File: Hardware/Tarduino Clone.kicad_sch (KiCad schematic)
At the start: 20 parts, among them J1 Conn_01x07_Male, J2 Conn_01x04_Male, J3 Conn_01x02_Male, J4 Conn_01x02_Male, J5 Conn_01x02_Male, J6 Conn_01x02_Male, J7 Conn_01x08_Male, J8 QWIIC_Vertical, J9 QWIIC_Stackable, SW1 SW_Push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

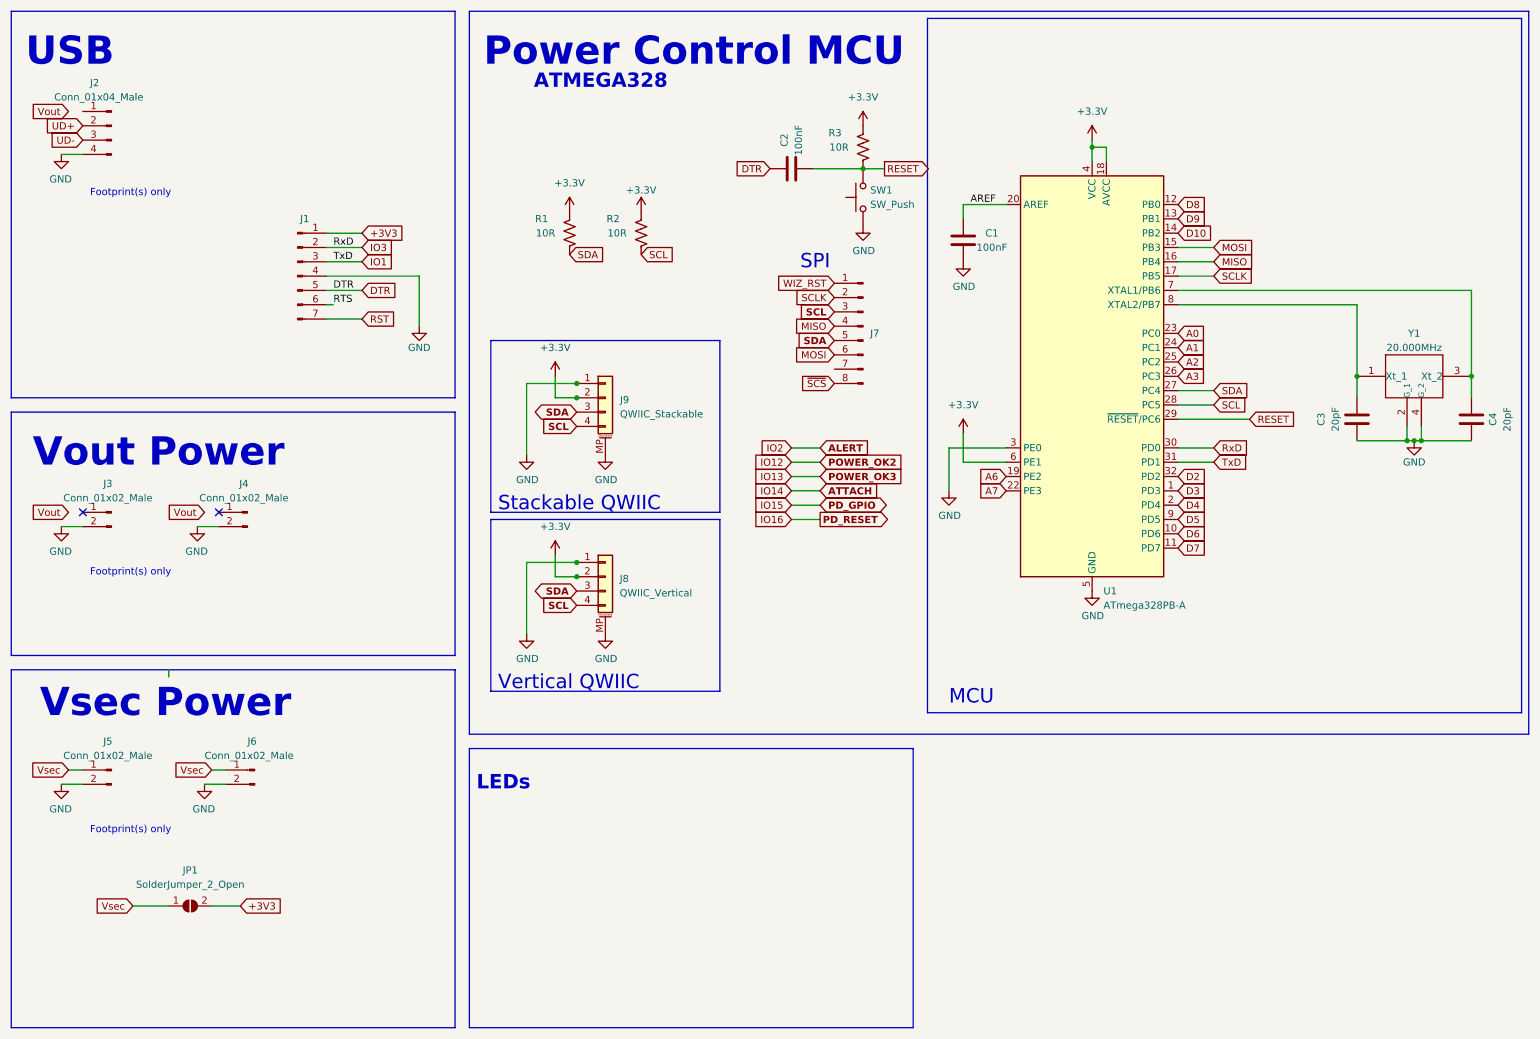
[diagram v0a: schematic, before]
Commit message: Still cleaning up J7
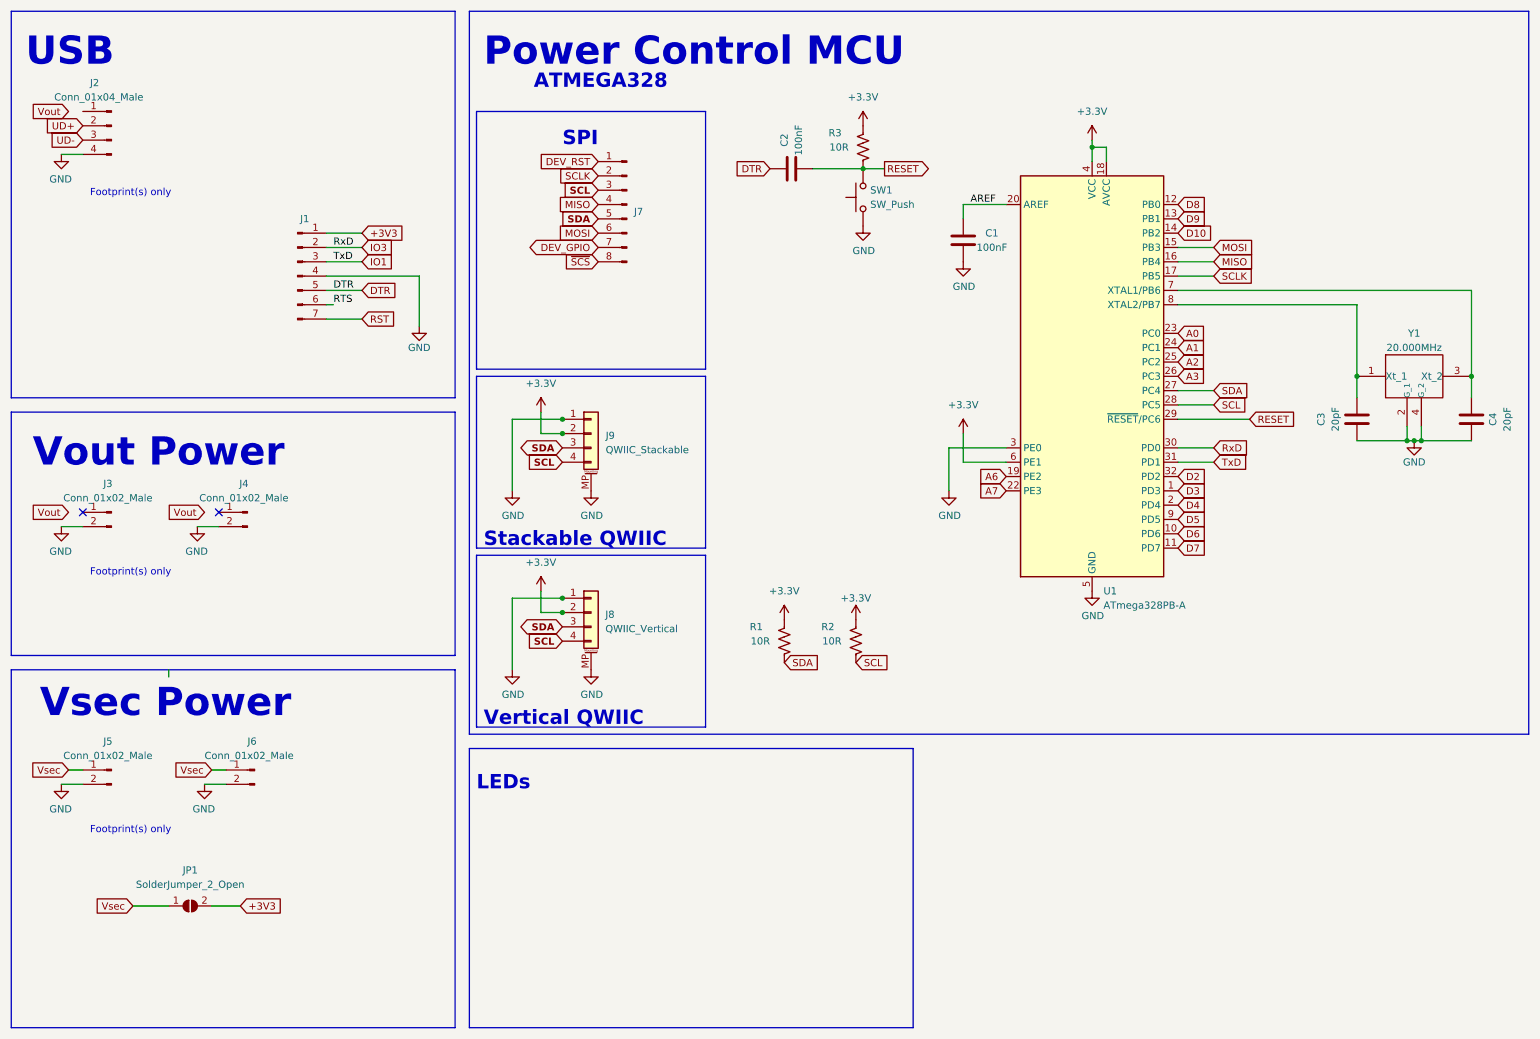
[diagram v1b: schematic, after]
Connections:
- net DEV_GPIO: now reaches J7.7 (Pin_7)
- net WIZ_RST renamed DEV_RST
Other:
- note removed: "MCU"
- moved on the sheet: J7, J8, J9, R1, R2
